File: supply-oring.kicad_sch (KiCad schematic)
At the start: 14 parts, among them U56 LTC4358CDE, U57 LTC4358CDE, U58 LTC4358CDE

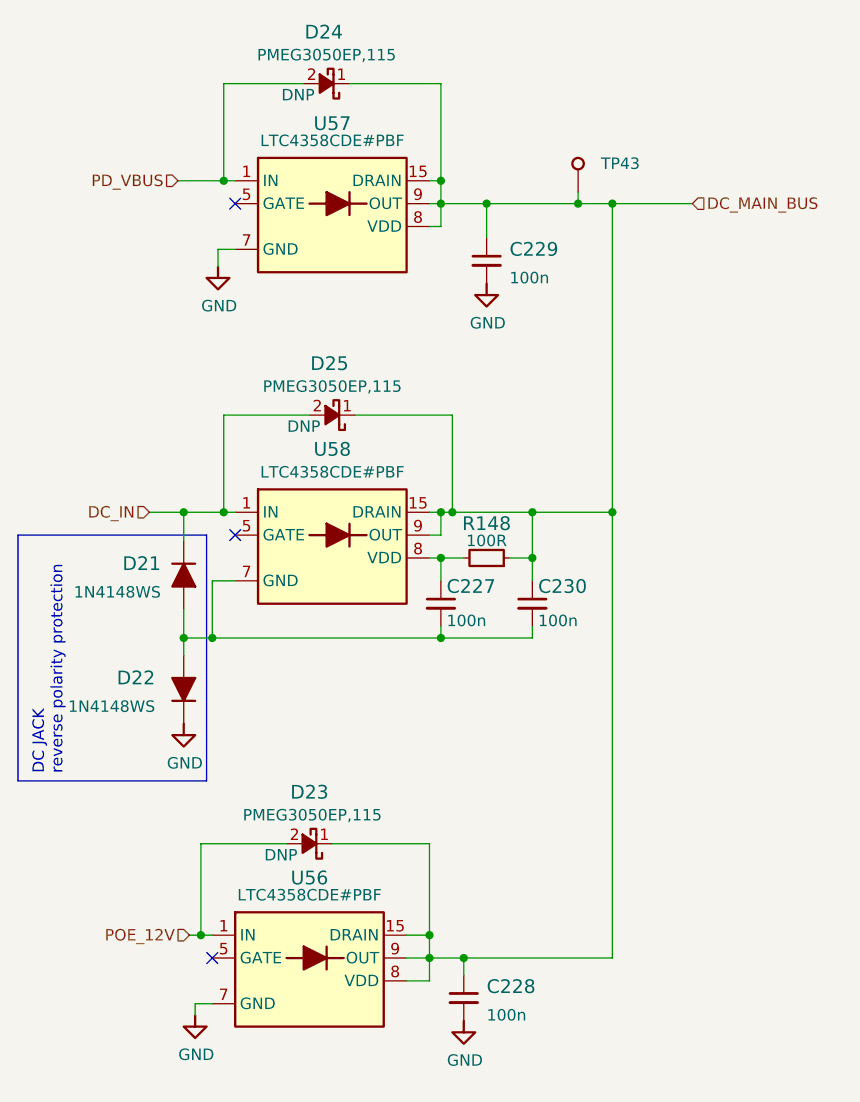
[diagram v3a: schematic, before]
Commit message: [#56935] Update symbol/footprint links; Migrate to KiCad 7
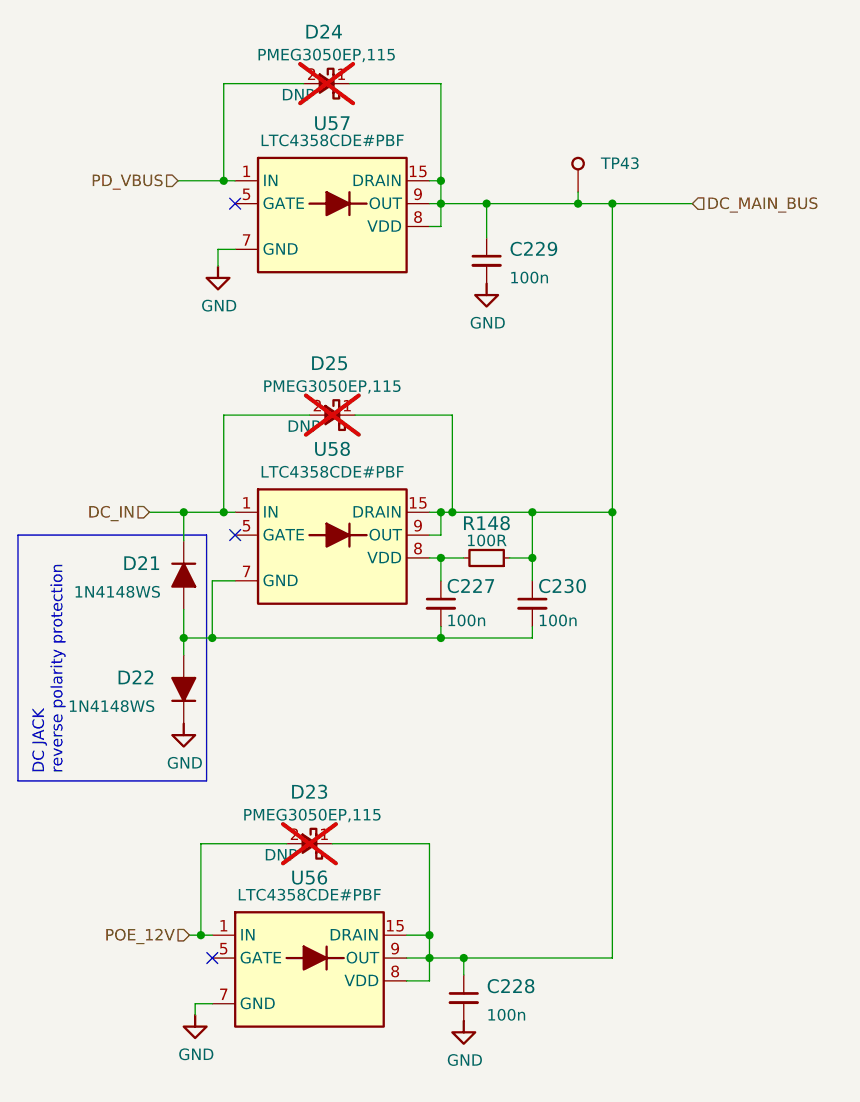
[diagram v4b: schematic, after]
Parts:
- C227, C228, C229, C230: footprint kria-k26-devboard-footprints:C_0402_1005Metric -> antmicro-footprints:C_0402_1005Metric; symbol kria-k26-devboard:C_100n_0402 -> antmicroCapacitors0402:C_100n_0402
- D21, D22: footprint kria-k26-devboard-footprints:D_SOD-323F -> antmicro-footprints:D_SOD-323F; symbol kria-k26-devboard:1N4148WS -> antmicroDiodesRectifiersSingle:1N4148WS
- D23, D24, D25: footprint kria-k26-devboard-footprints:Nexperia_SOD128 -> antmicro-footprints:Nexperia_SOD128; symbol kria-k26-devboard:PMEG3050EP,115 -> antmicroDiodesRectifiersSingle:PMEG3050EP,115; now not fitted; now left out of the parts list
- R148: footprint kria-k26-devboard-footprints:R_0402_1005Metric -> antmicro-footprints:R_0402_1005Metric; symbol kria-k26-devboard:R_100R_0402 -> antmicroResistors0402:R_100R_0402
- TP43: footprint kria-k26-devboard-footprints:TP_SMD_0.75mm -> antmicro-footprints:TP_SMD_0.75mm; symbol kria-k26-devboard:TP_0.75mm_SMD -> antmicroTestPoints:TP_0.75mm_SMD
- U56, U57, U58: footprint kria-k26-devboard-footprints:DFN-14-1EP_4x3mm_P0.5mm -> antmicro-footprints:DFN-14-1EP_4x3mm_P0.5mm; symbol kria-k26-devboard:LTC4358CDE -> antmicroPMICORControllersIdealDiodes:LTC4358CDE

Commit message: [#56935] Fix missing highlights in OHP
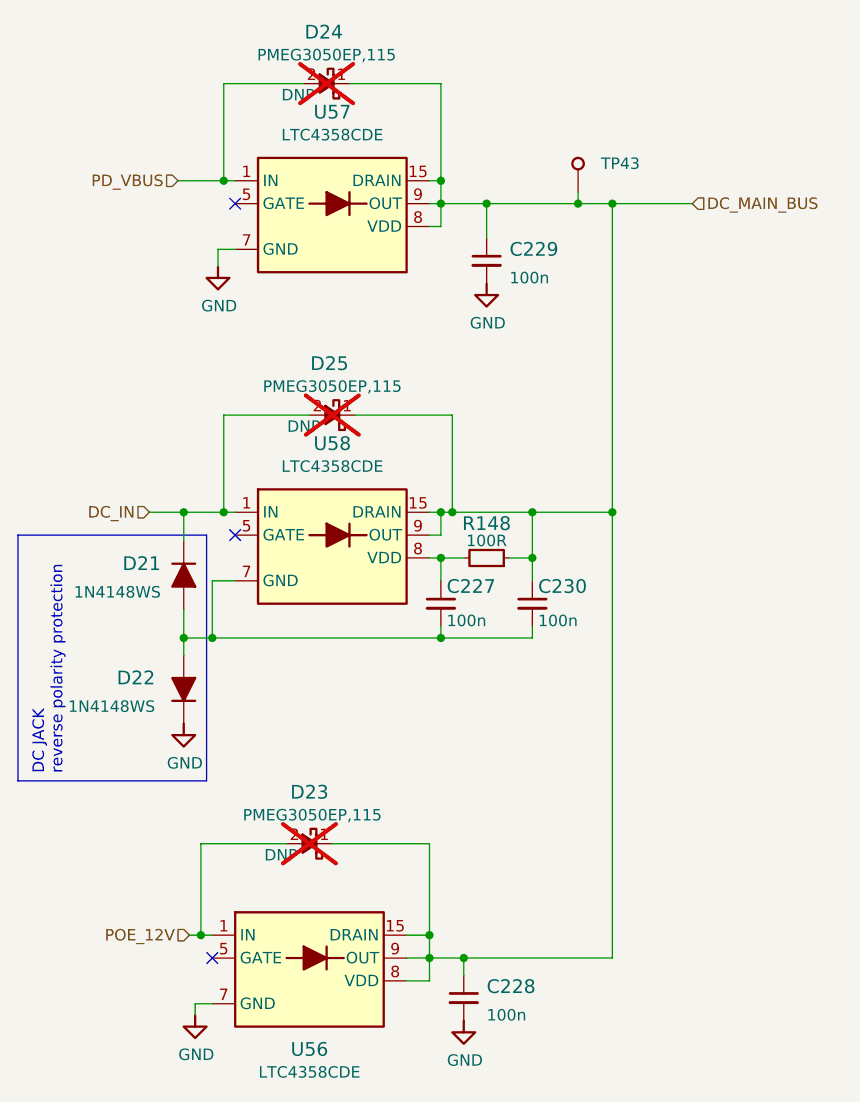
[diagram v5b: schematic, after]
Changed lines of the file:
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@@
   )
   (symbol (lib_id "antmicroPMICORControllersIdealDiodes:LTC4358CDE") (at 128.27 57.15 0) (unit 1)
-    (in_bom yes) (on_board yes) (dnp no)
-    (property "Reference" "U57" (at 139.065 50.8 0)
+    (in_bom yes) (on_board yes) (dnp no) (fields_autoplaced)
+    (property "Reference" "U57" (at 139.065 49.53 0)
       (effects (font (size 1.524 1.524)))
     )
     (property "Value" "LTC4358CDE" (at 139.065 52.07 0)
+      (effects (font (size 1.27 1.27) (thickness 0.15)))
+    )
+    (property "Footprint" "antmicro-footprints:DFN-14-1EP_4x3mm_P0.5mm" (at 137.16 37.084 0)
+      (effects (font (size 1.27 1.27) (thickness 0.15)) (justify left bottom) hide)
+    )
+    (property "Datasheet" "https://www.mouser.com/datasheet/2/609/4358fa-1270155.pdf" (at 125.73 41.91 0)
+      (effects (font (size 1.27 1.27) (thickness 0.15)) (justify left bottom) hide)
+    )
+    (property "Manufacturer" "Analog Devices" (at 137.16 36.83 0)
+      (effects (font (size 1.27 1.27) (thickness 0.15)) (justify left bottom) hide)
+    )
+    (property "MPN" "LTC4358CDE#PBF" (at 139.065 52.705 0)
       (effects (font (size 1.27 1.27) (thickness 0.15)) hide)
-    )
-    (property "Footprint" "antmicro-footprints:DFN-14-1EP_4x3mm_P0.5mm" (at 137.16 37.084 0)
-      (effects (font (size 1.27 1.27) (thickness 0.15)) (justify left bottom) hide)
-    )
-    (property "Datasheet" "https://www.mouser.pl/datasheet/2/609/4358fa-1270155.pdf" (at 125.73 41.91 0)
-      (effects (font (size 1.27 1.27) (thickness 0.15)) (justify left bottom) hide)
-    )
-    (property "Manufacturer" "Analog Devices" (at 137.16 36.83 0)
-      (effects (font (size 1.27 1.27) (thickness 0.15)) (justify left bottom) hide)
-    )
-    (property "MPN" "LTC4358CDE#PBF" (at 139.065 52.705 0)
-      (effects (font (size 1.27 1.27) (thickness 0.15)))
     )
     (property "Author" "Antmicro" (at 163.83 74.93 0)
@@
   )
   (symbol (lib_id "antmicroPMICORControllersIdealDiodes:LTC4358CDE") (at 128.27 93.98 0) (unit 1)
-    (in_bom yes) (on_board yes) (dnp no)
-    (property "Reference" "U58" (at 139.065 86.995 0)
+    (in_bom yes) (on_board yes) (dnp no) (fields_autoplaced)
+    (property "Reference" "U58" (at 139.065 86.36 0)
       (effects (font (size 1.524 1.524)))
     )
-    (property "Value" "LTC4358CDE" (at 135.89 74.1426 0)
-      (effects (font (size 1.27 1.27) (thickness 0.15)) (justify left bottom) hide)
+    (property "Value" "LTC4358CDE" (at 139.065 88.9 0)
+      (effects (font (size 1.27 1.27) (thickness 0.15)))
     )
     (property "Footprint" "antmicro-footprints:DFN-14-1EP_4x3mm_P0.5mm" (at 137.16 73.914 0)
       (effects (font (size 1.27 1.27) (thickness 0.15)) (justify left bottom) hide)
     )
-    (property "Datasheet" "https://www.mouser.pl/datasheet/2/609/4358fa-1270155.pdf" (at 125.73 78.74 0)
+    (property "Datasheet" "https://www.mouser.com/datasheet/2/609/4358fa-1270155.pdf" (at 125.73 78.74 0)
       (effects (font (size 1.27 1.27) (thickness 0.15)) (justify left bottom) hide)
     )
@@
     )
     (property "MPN" "LTC4358CDE#PBF" (at 139.065 89.535 0)
-      (effects (font (size 1.27 1.27) (thickness 0.15)))
+      (effects (font (size 1.27 1.27) (thickness 0.15)) hide)
     )
     (property "Author" "Antmicro" (at 163.83 111.76 0)
@@
   )
   (symbol (lib_id "antmicroPMICORControllersIdealDiodes:LTC4358CDE") (at 125.73 140.97 0) (unit 1)
-    (in_bom yes) (on_board yes) (dnp no)
-    (property "Reference" "U56" (at 136.525 134.62 0)
+    (in_bom yes) (on_board yes) (dnp no) (fields_autoplaced)
+    (property "Reference" "U56" (at 136.525 153.67 0)
       (effects (font (size 1.524 1.524)))
     )
-    (property "Value" "LTC4358CDE" (at 133.35 121.1326 0)
-      (effects (font (size 1.27 1.27) (thickness 0.15)) (justify left bottom) hide)
+    (property "Value" "LTC4358CDE" (at 136.525 156.21 0)
+      (effects (font (size 1.27 1.27) (thickness 0.15)))
     )
     (property "Footprint" "antmicro-footprints:DFN-14-1EP_4x3mm_P0.5mm" (at 134.62 120.904 0)
       (effects (font (size 1.27 1.27) (thickness 0.15)) (justify left bottom) hide)
     )
-    (property "Datasheet" "https://www.mouser.pl/datasheet/2/609/4358fa-1270155.pdf" (at 123.19 125.73 0)
+    (property "Datasheet" "https://www.mouser.com/datasheet/2/609/4358fa-1270155.pdf" (at 123.19 125.73 0)
       (effects (font (size 1.27 1.27) (thickness 0.15)) (justify left bottom) hide)
     )
@@
     )
     (property "MPN" "LTC4358CDE#PBF" (at 136.525 136.525 0)
-      (effects (font (size 1.27 1.27) (thickness 0.15)))
+      (effects (font (size 1.27 1.27) (thickness 0.15)) hide)
     )
     (property "Author" "Antmicro" (at 161.29 158.75 0)

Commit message: [#56935] Loclib
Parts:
- C227, C228, C229, C230: footprint antmicro-footprints:C_0402_1005Metric -> kria-k26-devboard-footprints:C_0402_1005Metric; symbol antmicroCapacitors0402:C_100n_0402 -> kria-k26-devboard:C_100n_0402
- D21, D22: footprint antmicro-footprints:D_SOD-323F -> kria-k26-devboard-footprints:D_SOD-323F; symbol antmicroDiodesRectifiersSingle:1N4148WS -> kria-k26-devboard:1N4148WS
- D23, D24, D25: footprint antmicro-footprints:Nexperia_SOD128 -> kria-k26-devboard-footprints:Nexperia_SOD128; symbol antmicroDiodesRectifiersSingle:PMEG3050EP,115 -> kria-k26-devboard:PMEG3050EP,115
- R148: footprint antmicro-footprints:R_0402_1005Metric -> kria-k26-devboard-footprints:R_0402_1005Metric; symbol antmicroResistors0402:R_100R_0402 -> kria-k26-devboard:R_100R_0402
- TP43: footprint antmicro-footprints:TP_SMD_0.75mm -> kria-k26-devboard-footprints:TP_SMD_0.75mm; symbol antmicroTestPoints:TP_0.75mm_SMD -> kria-k26-devboard:TP_0.75mm_SMD
- U56, U57, U58: footprint antmicro-footprints:DFN-14-1EP_4x3mm_P0.5mm -> kria-k26-devboard-footprints:DFN-14-1EP_4x3mm_P0.5mm; symbol antmicroPMICORControllersIdealDiodes:LTC4358CDE -> kria-k26-devboard:LTC4358CDE
